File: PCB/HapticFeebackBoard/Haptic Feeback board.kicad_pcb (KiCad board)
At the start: 2 copper layers, 12 parts, among them J1 1769, J2 Conn_01x02, J3 Conn_01x02, J4 Conn_01x02, Q1 2N7002E, SW1 PTS526 SM15 SMTR2 LFS

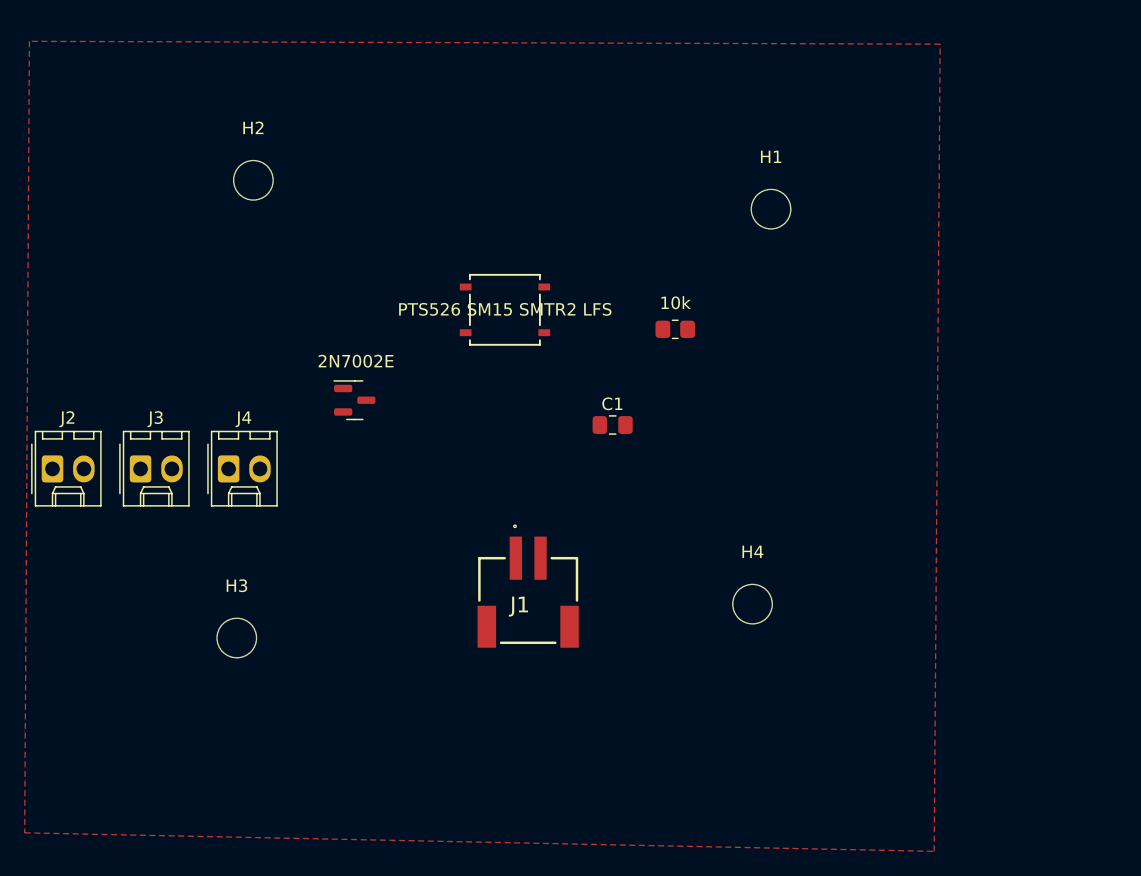
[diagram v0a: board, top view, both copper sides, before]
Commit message: Finished Haptic Feedback Board
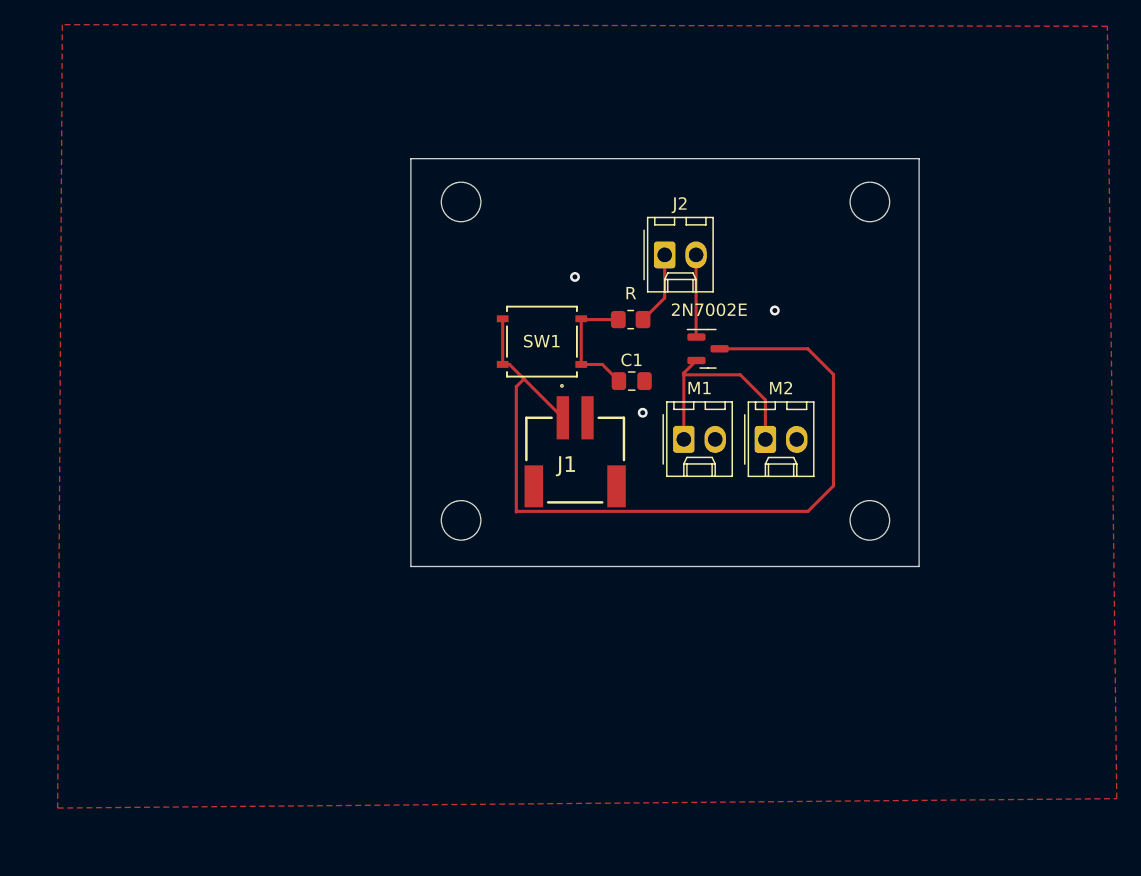
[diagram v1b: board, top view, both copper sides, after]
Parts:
- R1: value 10k -> R
- moved J2 52.5 mm to (141.0, 87.5)
- moved M2 50.6 mm to (149.1, 102.4)
- moved M1 36.9 mm to (142.5, 102.4)
- moved Q1 28.9 mm to (144.5, 95.1)
- moved H3 20.5 mm to (124.5, 109.0)
- moved H2 16.9 mm to (124.5, 83.2)
- moved J1 12.0 mm to (133.7, 100.7)
- moved H4 11.7 mm to (157.6, 109.0)
- moved H1 8.02 mm to (157.6, 83.2)
- moved SW1 3.95 mm to (131.1, 94.5)
- moved C1 3.88 mm to (138.3, 97.7)
- moved R1 3.69 mm to (138.2, 92.7)
- renumbered J4 to M1, J3 to M2
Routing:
- net /BMS Power: track 0.00 -> 67.0 mm
- net /Motor1: track 0.00 -> 17.5 mm
- net Net-(C1-Pad1): track 0.00 -> 10.3 mm
- net /GPIO: track 0.00 -> 6.66 mm
- net /MCU: track 0.00 -> 5.96 mm
- net GND: vias 0 -> 3
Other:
- board outline added: 41.1 x 33 mm

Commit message: Revert "Finished Haptic Feedback Board"
This reverts commit e00eed14296bda41403d05f06b408ec44583351d.
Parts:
- R1: value R -> 10k
- moved J2 52.5 mm to (91.4, 104.8)
- moved J3 50.6 mm to (98.6, 104.8)
- moved J4 36.9 mm to (105.7, 104.8)
- moved Q1 28.9 mm to (115.9, 99.3)
- moved H3 20.5 mm to (106.3, 118.5)
- moved H2 16.9 mm to (107.7, 81.5)
- moved J1 12.0 mm to (129.9, 112.1)
- moved H4 11.7 mm to (148.1, 115.8)
- moved H1 8.02 mm to (149.6, 83.8)
- moved SW1 3.95 mm to (128.1, 91.9)
- moved C1 3.88 mm to (136.8, 101.3)
- moved R1 3.69 mm to (141.8, 93.5)
- renumbered M2 to J3, M1 to J4
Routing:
- net /BMS Power: track 67.0 -> 0.00 mm
- net /Motor1: track 17.5 -> 0.00 mm
- net Net-(C1-Pad1): track 10.3 -> 0.00 mm
- net /GPIO: track 6.66 -> 0.00 mm
- net /MCU: track 5.96 -> 0.00 mm
- net GND: vias 3 -> 0
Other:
- board outline removed

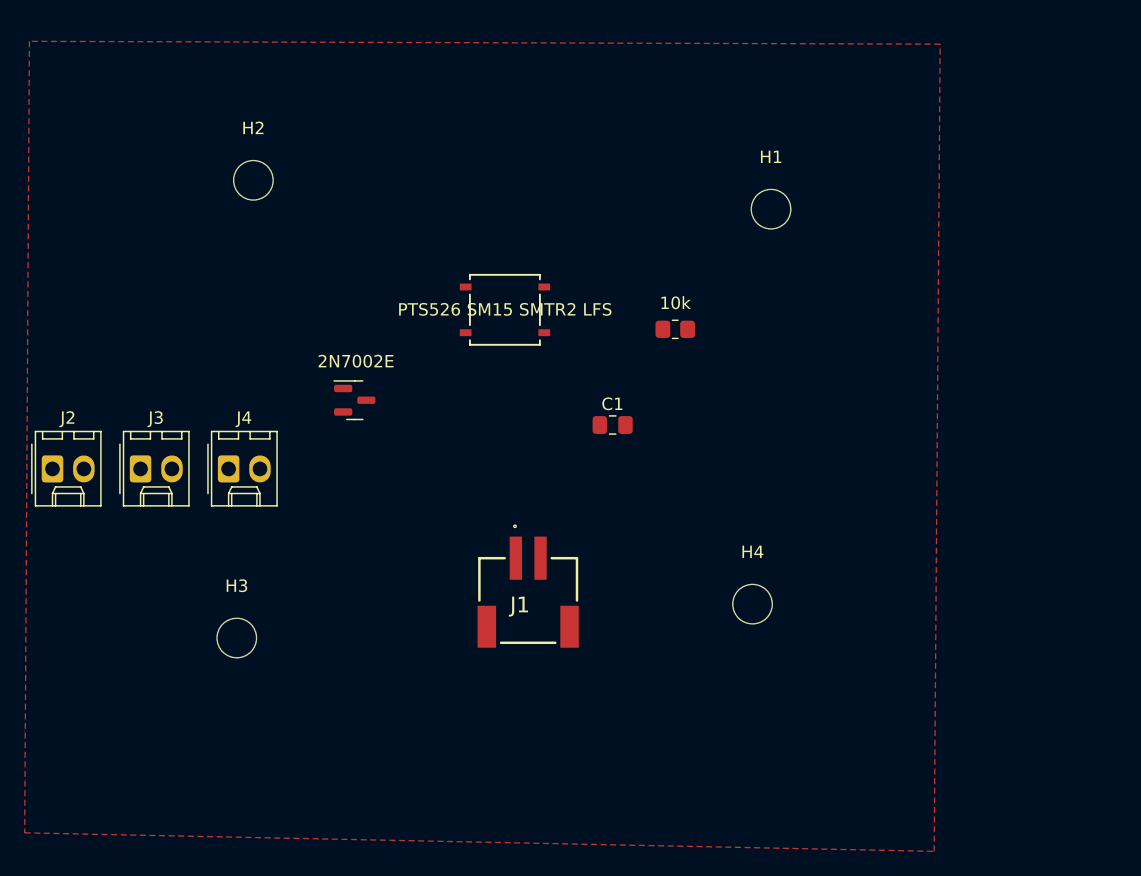
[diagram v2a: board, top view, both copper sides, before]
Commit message: Pushing Haptic Feedback
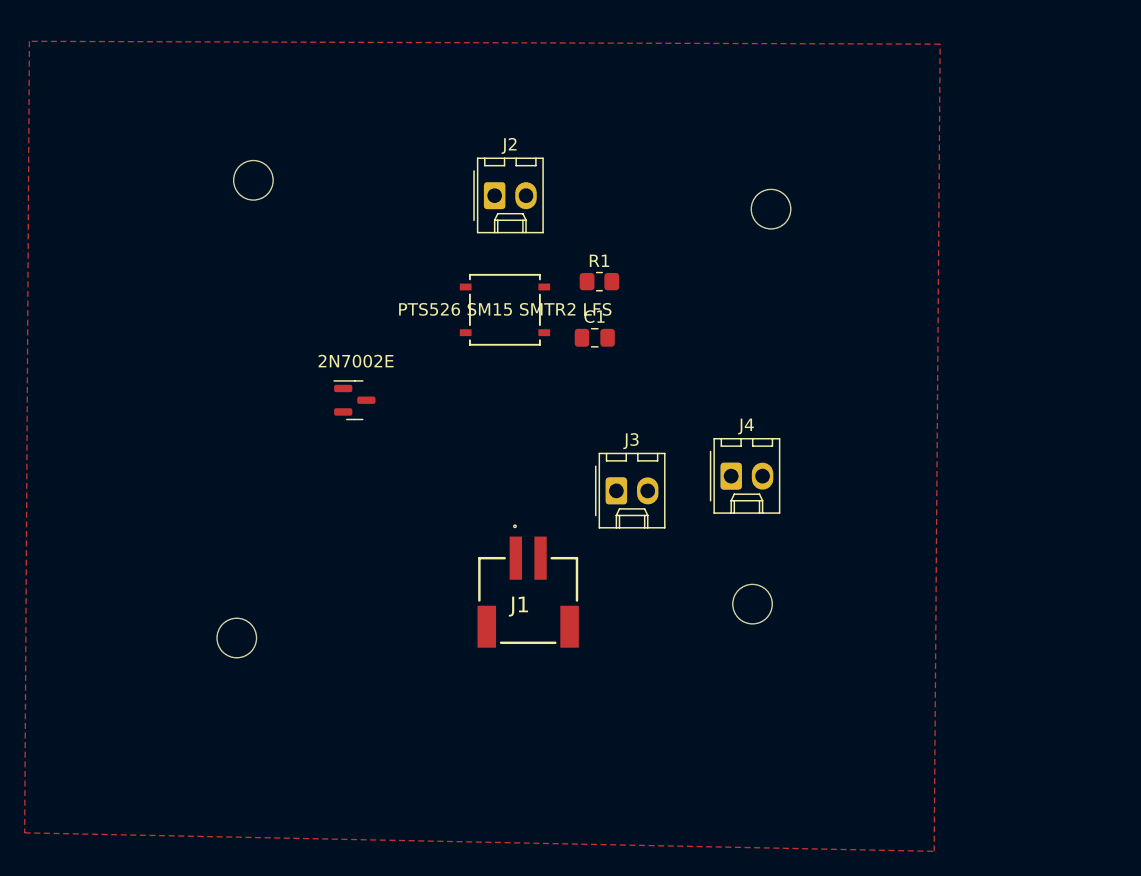
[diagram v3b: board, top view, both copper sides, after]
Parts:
- moved J2 42.1 mm to (127.2, 82.7)
- moved J4 40.7 mm to (146.4, 105.4)
- moved J3 38.6 mm to (137.1, 106.6)
- moved R1 7.25 mm to (135.7, 89.7)
- moved C1 7.21 mm to (135.3, 94.2)
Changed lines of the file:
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@@
   )
   (setup
+    (stackup
+      (layer "F.SilkS" (type "Top Silk Screen"))
+      (layer "F.Paste" (type "Top Solder Paste"))
+      (layer "F.Mask" (type "Top Solder Mask") (thickness 0.01))
+      (layer "F.Cu" (type "copper") (thickness 0.035))
+      (layer "dielectric 1" (type "core") (thickness 1.51) (material "FR4") (epsilon_r 4.5) (loss_tangent 0.02))
+      (layer "B.Cu" (type "copper") (thickness 0.035))
+      (layer "B.Mask" (type "Bottom Solder Mask") (thickness 0.01))
+      (layer "B.Paste" (type "Bottom Solder Paste"))
+      (layer "B.SilkS" (type "Bottom Silk Screen"))
+      (copper_finish "None")
+      (dielectric_constraints no)
+    )
     (pad_to_mask_clearance 0)
     (pcbplotparams
@@
     (property "ki_keywords" "mounting hole")
     (attr exclude_from_pos_files)
-    (fp_text reference "H3" (at 0 -4.2) (layer "F.SilkS")
-        (effects (font (size 1 1) (thickness 0.15)))
-    )
-    (fp_text value "MountingHole" (at 0 4.2) (layer "F.Fab")
-        (effects (font (size 1 1) (thickness 0.15)))
-    )
-    (fp_text user "${REFERENCE}" (at 0.6858 0.5078) (layer "F.Fab")
+    (fp_text reference "H3" (at 0 -4.2) (layer "F.SilkS") hide
+        (effects (font (size 1 1) (thickness 0.15)))
+    )
+    (fp_text value "MountingHole" (at 0 4.2) (layer "F.Fab") hide
+        (effects (font (size 1 1) (thickness 0.15)))
+    )
+    (fp_text user "${REFERENCE}" (at 0.6858 0.5078) (layer "F.Fab") hide
         (effects (font (size 1 1) (thickness 0.15)))
     )
@@
     (property "ki_keywords" "mounting hole")
     (attr exclude_from_pos_files)
-    (fp_text reference "H2" (at 0 -4.2) (layer "F.SilkS")
-        (effects (font (size 1 1) (thickness 0.15)))
-    )
-    (fp_text value "MountingHole" (at 0 4.2) (layer "F.Fab")
-        (effects (font (size 1 1) (thickness 0.15)))
-    )
-    (fp_text user "${REFERENCE}" (at 0 0) (layer "F.Fab")
+    (fp_text reference "H2" (at 0 -4.2) (layer "F.SilkS") hide
+        (effects (font (size 1 1) (thickness 0.15)))
+    )
+    (fp_text value "MountingHole" (at 0 4.2) (layer "F.Fab") hide
+        (effects (font (size 1 1) (thickness 0.15)))
+    )
+    (fp_text user "${REFERENCE}" (at 0 0) (layer "F.Fab") hide
         (effects (font (size 1 1) (thickness 0.15)))
     )
@@
   )
   (footprint "Capacitor_SMD:C_0805_2012Metric_Pad1.18x1.45mm_HandSolder" (layer "F.Cu")
-    (at 136.7829 101.2698)
+    (at 135.3351 94.2086)
     (descr "Capacitor SMD 0805 (2012 Metric), square (rectangular) end terminal, IPC_7351 nominal with elongated pad for handsoldering. (Body size source: IPC-SM-782 page 76, https://www.pcb-3d.com/wordpress/wp-content/uploads/ipc-sm-782a_amendment_1_and_2.pdf, https://docs.google.com/spreadsheets/d/1BsfQQcO9C6DZCsRaXUlFlo91Tg2WpOkGARC1WS5S8t0/edit?usp=sharing), generated with kicad-footprint-generator")
     (tags "capacitor handsolder")
@@
         (effects (font (size 1 1) (thickness 0.15)))
     )
-    (fp_text value "1uF" (at 0 1.68) (layer "F.Fab")
-        (effects (font (size 1 1) (thickness 0.15)))
-    )
-    (fp_text user "${REFERENCE}" (at 0 0) (layer "F.Fab")
+    (fp_text value "1uF" (at 0 1.68) (layer "F.Fab") hide
+        (effects (font (size 1 1) (thickness 0.15)))
+    )
+    (fp_text user "${REFERENCE}" (at 0 0) (layer "F.Fab") hide
         (effects (font (size 0.5 0.5) (thickness 0.08)))
     )
@@
     (property "ki_keywords" "mounting hole")
     (attr exclude_from_pos_files)
-    (fp_text reference "H4" (at 0 -4.2) (layer "F.SilkS")
-        (effects (font (size 1 1) (thickness 0.15)))
-    )
-    (fp_text value "MountingHole" (at 0 4.2) (layer "F.Fab")
-        (effects (font (size 1 1) (thickness 0.15)))
-    )
-    (fp_text user "${REFERENCE}" (at 0.2286 0.127) (layer "F.Fab")
+    (fp_text reference "H4" (at 0 -4.2) (layer "F.SilkS") hide
+        (effects (font (size 1 1) (thickness 0.15)))
+    )
+    (fp_text value "MountingHole" (at 0 4.2) (layer "F.Fab") hide
+        (effects (font (size 1 1) (thickness 0.15)))
+    )
+    (fp_text user "${REFERENCE}" (at 0.2286 0.127) (layer "F.Fab") hide
         (effects (font (size 1 1) (thickness 0.15)))
     )
@@
   )
   (footprint "Connector_Molex:Molex_KK-254_AE-6410-02A_1x02_P2.54mm_Vertical" (layer "F.Cu")
-    (at 91.4294 104.8258)
+    (at 127.2286 82.7024)
     (descr "Molex KK-254 Interconnect System, old/engineering part number: AE-6410-02A example for new part number: 22-27-2021, 2 Pins (http://www.molex.com/pdm_docs/sd/022272021_sd.pdf), generated with kicad-footprint-generator")
     (tags "connector Molex KK-254 vertical")
@@
     (property "ki_keywords" "mounting hole")
     (attr exclude_from_pos_files)
-    (fp_text reference "H1" (at 0 -4.2) (layer "F.SilkS")
-        (effects (font (size 1 1) (thickness 0.15)))
-    )
-    (fp_text value "MountingHole" (at 0 4.2) (layer "F.Fab")
-        (effects (font (size 1 1) (thickness 0.15)))
-    )
-    (fp_text user "${REFERENCE}" (at 0 0) (layer "F.Fab")
+    (fp_text reference "H1" (at 0 -4.2) (layer "F.SilkS") hide
+        (effects (font (size 1 1) (thickness 0.15)))
+    )
+    (fp_text value "MountingHole" (at 0 4.2) (layer "F.Fab") hide
+        (effects (font (size 1 1) (thickness 0.15)))
+    )
+    (fp_text user "${REFERENCE}" (at 0 0) (layer "F.Fab") hide
         (effects (font (size 1 1) (thickness 0.15)))
     )
@@
   )
   (footprint "Connector_Molex:Molex_KK-254_AE-6410-02A_1x02_P2.54mm_Vertical" (layer "F.Cu")
-    (at 98.5594 104.8258)
+    (at 137.0838 106.6038)
     (descr "Molex KK-254 Interconnect System, old/engineering part number: AE-6410-02A example for new part number: 22-27-2021, 2 Pins (http://www.molex.com/pdm_docs/sd/022272021_sd.pdf), generated with kicad-footprint-generator")
     (tags "connector Molex KK-254 vertical")
@@
   )
   (footprint "Connector_Molex:Molex_KK-254_AE-6410-02A_1x02_P2.54mm_Vertical" (layer "F.Cu")
-    (at 105.6894 104.8258)
+    (at 146.3802 105.41)
     (descr "Molex KK-254 Interconnect System, old/engineering part number: AE-6410-02A example for new part number: 22-27-2021, 2 Pins (http://www.molex.com/pdm_docs/sd/022272021_sd.pdf), generated with kicad-footprint-generator")
     (tags "connector Molex KK-254 vertical")
@@
   )
   (footprint "Resistor_SMD:R_0805_2012Metric_Pad1.20x1.40mm_HandSolder" (layer "F.Cu")
-    (at 141.8496 93.5228)
+    (at 135.7122 89.662)
     (descr "Resistor SMD 0805 (2012 Metric), square (rectangular) end terminal, IPC_7351 nominal with elongated pad for handsoldering. (Body size source: IPC-SM-782 page 72, https://www.pcb-3d.com/wordpress/wp-content/uploads/ipc-sm-782a_amendment_1_and_2.pdf), generated with kicad-footprint-generator")
     (tags "resistor handsolder")
@@
     (property "ki_keywords" "R res resistor")
     (attr smd)
-    (fp_text reference "R1" (at 0 -1.65) (layer "F.SilkS") hide
-        (effects (font (size 1 1) (thickness 0.15)))
-    )
-    (fp_text value "10k" (at 0 -2.1082) (layer "F.SilkS")
-        (effects (font (size 1 1) (thickness 0.15)))
-    )
-    (fp_text user "${REFERENCE}" (at 0 0) (layer "F.Fab")
+    (fp_text reference "R1" (at 0 -1.65) (layer "F.SilkS")
+        (effects (font (size 1 1) (thickness 0.15)))
+    )
+    (fp_text value "10k" (at 0 -2.1082) (layer "F.SilkS") hide
+        (effects (font (size 1 1) (thickness 0.15)))
+    )
+    (fp_text user "${REFERENCE}" (at 0 0) (layer "F.Fab") hide
         (effects (font (size 0.5 0.5) (thickness 0.08)))
     )

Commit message: Recovery attempt 2
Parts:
- removed C1: 1uF, Capacitor_SMD:C_0805_2012Metric_Pad1.18x1.45mm_HandSolder
- removed H1, H2, H3, H4: MountingHole, MountingHole:MountingHole_3.2mm_M3
- removed J1: 1769, Adafruit Accessories JST-PH 2-pin SMT Right Angle Connect:1769
- removed J2, J3, J4: Conn_01x02, Connector_Molex:Molex_KK-254_AE-6410-02A_1x02_P2.54mm_Vertical
- removed Q1: 2N7002E, Package_TO_SOT_SMD:SOT-23
- removed R1: 10k, Resistor_SMD:R_0805_2012Metric_Pad1.20x1.40mm_HandSolder
- removed SW1: PTS526 SM15 SMTR2 LFS, PTS526 SM15 SMTR2 LFS:SON4_PTS526 SM15 SMTR2 LFS_CNK
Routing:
- removed copper zone on F.Cu, net GND

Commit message: Updating Haptic Feedback Board
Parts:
- added C1: 1uF, Capacitor_SMD:C_0805_2012Metric_Pad1.18x1.45mm_HandSolder, F.Cu at (138.3, 97.7)
- added H1: MountingHole, MountingHole:MountingHole_3.2mm_M3, F.Cu at (157.6, 83.2)
- added H2: MountingHole, MountingHole:MountingHole_3.2mm_M3, F.Cu at (124.5, 83.2)
- added H3: MountingHole, MountingHole:MountingHole_3.2mm_M3, F.Cu at (124.5, 109.0)
- added H4: MountingHole, MountingHole:MountingHole_3.2mm_M3, F.Cu at (157.6, 109.0)
- added J1: 1769, Adafruit Accessories JST-PH 2-pin SMT Right Angle Connect:1769, F.Cu at (133.7, 100.7)
- added J2: Conn_01x02, Connector_Molex:Molex_KK-254_AE-6410-02A_1x02_P2.54mm_Vertical, F.Cu at (141.0, 87.5)
- added M1: Conn_01x02, Connector_Molex:Molex_KK-254_AE-6410-02A_1x02_P2.54mm_Vertical, F.Cu at (142.5, 102.4)
- added M2: Conn_01x02, Connector_Molex:Molex_KK-254_AE-6410-02A_1x02_P2.54mm_Vertical, F.Cu at (149.1, 102.4)
- added Q1: 2N7002E, Package_TO_SOT_SMD:SOT-23, F.Cu at (144.5, 95.1)
- added R1: R, Resistor_SMD:R_0805_2012Metric_Pad1.20x1.40mm_HandSolder, F.Cu at (138.2, 92.7)
- added SW1: PTS526 SM15 SMTR2 LFS, PTS526 SM15 SMTR2 LFS:SON4_PTS526 SM15 SMTR2 LFS_CNK, F.Cu at (131.1, 94.5)
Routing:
- net /BMS Power: track 0.00 -> 67.0 mm
- net /Motor1: track 0.00 -> 17.5 mm
- net Net-(C1-Pad1): track 0.00 -> 10.3 mm
- net /GPIO: track 0.00 -> 6.66 mm
- net /MCU: track 0.00 -> 5.96 mm
- added copper zone on F.Cu, net GND

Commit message: Edits to Haptic Feedback
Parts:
- moved H4 3.21 mm to (156.5, 112.0)
- moved H3 3.17 mm to (125.5, 112.0)
- moved H1 1.13 mm to (156.5, 83.0)
- moved H2 1.01 mm to (125.5, 83.0)
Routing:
- net Net-(C1-Pad1): track 10.3 -> 6.64 mm
- net /BMS Power: track 67.0 -> 69.7 mm
- net /Motor1: track 17.5 -> 15.6 mm
- net GND: vias 0 -> 3
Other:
- board outline added: 43.5 x 37.5 mm
